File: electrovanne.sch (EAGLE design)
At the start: 11 parts, among them T1 2N2222, T2 2N2222, X1 MKDSN1,5/2-5,08

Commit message: enhanvced version
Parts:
- removed U$3: 709-SMU02N-05, mouser:709-SMU02N-05
- added C1: 0.68uF, SparkFun-Capacitors:CAP0603-CAP
- added IC1: 7805TV, linear:7805TV
- added R5: 10k, resistor:R-US_R0603
- R1: device resistor:R-EU_0207/10 -> resistor:R-US_R0603
- R2: value (none) -> 10k; device resistor:R-US_0207/10 -> resistor:R-US_R0603
- R3: value (none) -> 200; device resistor:R-US_0207/10 -> resistor:R-US_R0603
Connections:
- removed net N$7: U$4.VREF
- new net N$5: R3.2, T2.E
- net GND: now also C1.2, IC1.GND, R3.1, R5.1; no longer R2.1, T2.E, U$3.VIN-, U$3.VO-
- net N$1: now also IC1.VI, R2.2, U$4.VREF; no longer R3.2, U$3.VIN+
- net N$2: now also R5.2; no longer R2.2
- net N$8: now also R2.1; no longer R3.1
- net VCC: now also C1.1, IC1.VO; no longer U$3.VO+
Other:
- moved on the sheet: R2, R3

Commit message: 2 bugfix: (EN): dont touch to it, + the H-Bridge2 bugfix: (EN): dont touch to it, + the H-Bridge
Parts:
- removed R3: 200, resistor:R-US_R0603
- added R4: 10k, resistor:R-US_R0603
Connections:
- removed net N$5: R3.2, T2.E
- new net N$7: MS1.GPIO6, R4.2, T1.B
- net GND: now also T2.E; no longer MS1.EN, R3.1
- net N$9: now also R4.1; no longer MS1.GPIO6, T1.B
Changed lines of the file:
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@@
 <part name="GND1" library="supply1" deviceset="GND" device=""/>
 <part name="GND2" library="supply1" deviceset="GND" device=""/>
-<part name="GND3" library="supply1" deviceset="GND" device=""/>
 <part name="U$2" library="mouser" deviceset="161-0725-E" device=""/>
 <part name="GND4" library="supply1" deviceset="GND" device=""/>
@@
 <part name="R5" library="resistor" deviceset="R-US_" device="R0603" value="10k"/>
 <part name="R2" library="resistor" deviceset="R-US_" device="R0603" value="10k"/>
-<part name="R3" library="resistor" deviceset="R-US_" device="R0603" value="200"/>
 <part name="R1" library="resistor" deviceset="R-US_" device="R0603" value="10k"/>
 <part name="IC1" library="linear" deviceset="78*" device="TV" technology="05"/>
@@
 <part name="C1" library="SparkFun-Capacitors" deviceset="CAP" device="0603-CAP" value="0.68uF"/>
 <part name="GND10" library="supply1" deviceset="GND" device=""/>
+<part name="R4" library="resistor" deviceset="R-US_" device="R0603" value="10k"/>
 </parts>
 <sheets>
@@
 <instance part="GND1" gate="1" x="55.88" y="53.34"/>
 <instance part="GND2" gate="1" x="71.12" y="53.34"/>
-<instance part="GND3" gate="1" x="5.08" y="63.5" rot="R180"/>
 <instance part="U$2" gate="G$1" x="88.9" y="-15.24"/>
 <instance part="GND4" gate="1" x="2.54" y="-25.4"/>
@@
 <instance part="T1" gate="G$1" x="50.8" y="-2.54"/>
 <instance part="T2" gate="G$1" x="27.94" y="2.54"/>
-<instance part="GND5" gate="1" x="30.48" y="-22.86"/>
+<instance part="GND5" gate="1" x="30.48" y="-5.08"/>
 <instance part="R5" gate="G$1" x="53.34" y="-12.7" rot="R90"/>
 <instance part="R2" gate="G$1" x="30.48" y="12.7" rot="R90"/>
-<instance part="R3" gate="G$1" x="30.48" y="-12.7" rot="R90"/>
 <instance part="R1" gate="G$1" x="60.96" y="45.72" rot="R90"/>
 <instance part="IC1" gate="A1" x="2.54" y="-12.7" rot="MR0"/>
@@
 <instance part="C1" gate="G$1" x="-12.7" y="-17.78"/>
 <instance part="GND10" gate="1" x="-12.7" y="-25.4"/>
+<instance part="R4" gate="G$1" x="7.62" y="2.54" rot="R180"/>
 </instances>
 <busses>
@@
 </segment>
 <segment>
-<pinref part="GND3" gate="1" pin="GND"/>
-<pinref part="MS1" gate="G$1" pin="EN"/>
-<wire x1="5.08" y1="60.96" x2="10.16" y2="60.96" width="0.1524" layer="91"/>
-</segment>
-<segment>
 <pinref part="GND4" gate="1" pin="GND"/>
 <wire x1="2.54" y1="-20.32" x2="2.54" y2="-22.86" width="0.1524" layer="91"/>
@@
 </segment>
 <segment>
-<pinref part="GND5" gate="1" pin="GND"/>
-<pinref part="R3" gate="G$1" pin="1"/>
-<wire x1="30.48" y1="-20.32" x2="30.48" y2="-17.78" width="0.1524" layer="91"/>
-</segment>
-<segment>
 <pinref part="R5" gate="G$1" pin="1"/>
 <pinref part="GND6" gate="1" pin="GND"/>
@@
 <pinref part="GND10" gate="1" pin="GND"/>
 <wire x1="-12.7" y1="-22.86" x2="-12.7" y2="-20.32" width="0.1524" layer="91"/>
+</segment>
+<segment>
+<pinref part="T2" gate="G$1" pin="E"/>
+<pinref part="GND5" gate="1" pin="GND"/>
 </segment>
 </net>
@@
 </segment>
 </net>
-<net name="N$9" class="0">
-<segment>
-<pinref part="T2" gate="G$1" pin="B"/>
-<wire x1="25.4" y1="-5.08" x2="25.4" y2="2.54" width="0.1524" layer="91"/>
-<wire x1="25.4" y1="2.54" x2="-15.24" y2="2.54" width="0.1524" layer="91"/>
+<net name="N$7" class="0">
+<segment>
+<pinref part="T1" gate="G$1" pin="B"/>
+<wire x1="45.72" y1="-2.54" x2="48.26" y2="-2.54" width="0.1524" layer="91"/>
+<wire x1="45.72" y1="-7.62" x2="45.72" y2="-2.54" width="0.1524" layer="91"/>
 <pinref part="MS1" gate="G$1" pin="GPIO6"/>
 <wire x1="10.16" y1="78.74" x2="-15.24" y2="78.74" width="0.1524" layer="91"/>
 <wire x1="-15.24" y1="78.74" x2="-15.24" y2="2.54" width="0.1524" layer="91"/>
-<wire x1="25.4" y1="-5.08" x2="45.72" y2="-5.08" width="0.1524" layer="91"/>
-<pinref part="T1" gate="G$1" pin="B"/>
-<wire x1="45.72" y1="-5.08" x2="45.72" y2="-2.54" width="0.1524" layer="91"/>
-<wire x1="45.72" y1="-2.54" x2="48.26" y2="-2.54" width="0.1524" layer="91"/>
-</segment>
-</net>
-<net name="N$5" class="0">
-<segment>
-<pinref part="T2" gate="G$1" pin="E"/>
-<wire x1="30.48" y1="-2.54" x2="30.48" y2="-7.62" width="0.1524" layer="91"/>
-<pinref part="R3" gate="G$1" pin="2"/>
-</segment>
-</net>
+<wire x1="-15.24" y1="2.54" x2="-15.24" y2="-7.62" width="0.1524" layer="91"/>
+<wire x1="45.72" y1="-7.62" x2="-15.24" y2="-7.62" width="0.1524" layer="91"/>
+<wire x1="-15.24" y1="2.54" x2="2.54" y2="2.54" width="0.1524" layer="91"/>
+<pinref part="R4" gate="G$1" pin="2"/>
+</segment>
+</net>
+<net name="N$9" class="0">
+<segment>
+<pinref part="R4" gate="G$1" pin="1"/>
+<pinref part="T2" gate="G$1" pin="B"/>
+<wire x1="12.7" y1="2.54" x2="25.4" y2="2.54" width="0.1524" layer="91"/>
+</segment>
+</net>

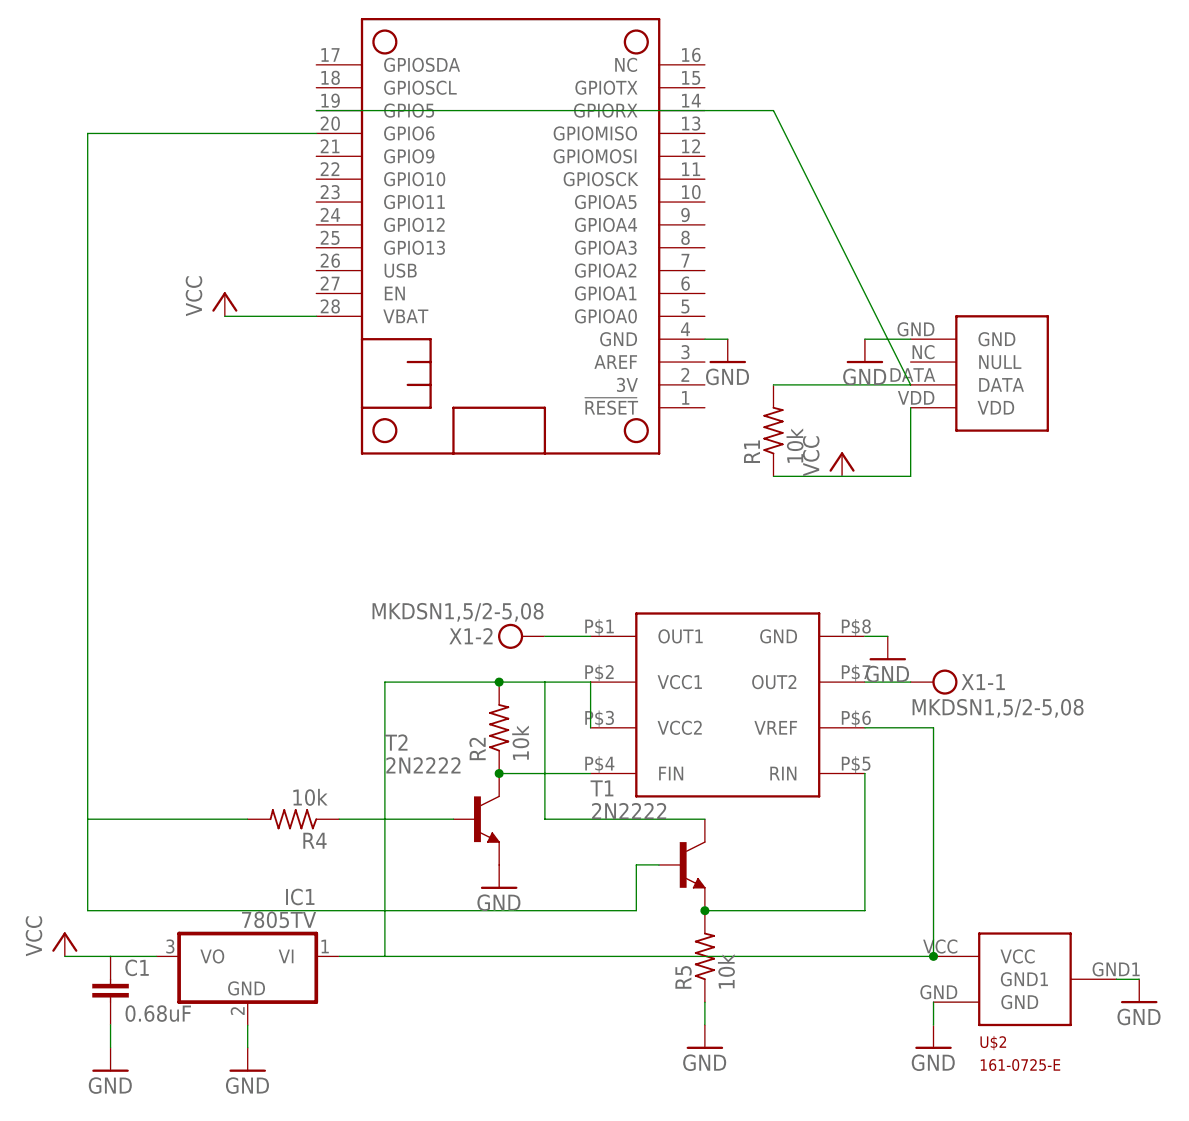
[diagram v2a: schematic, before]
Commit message: add small resistor (recommended by datasheet)
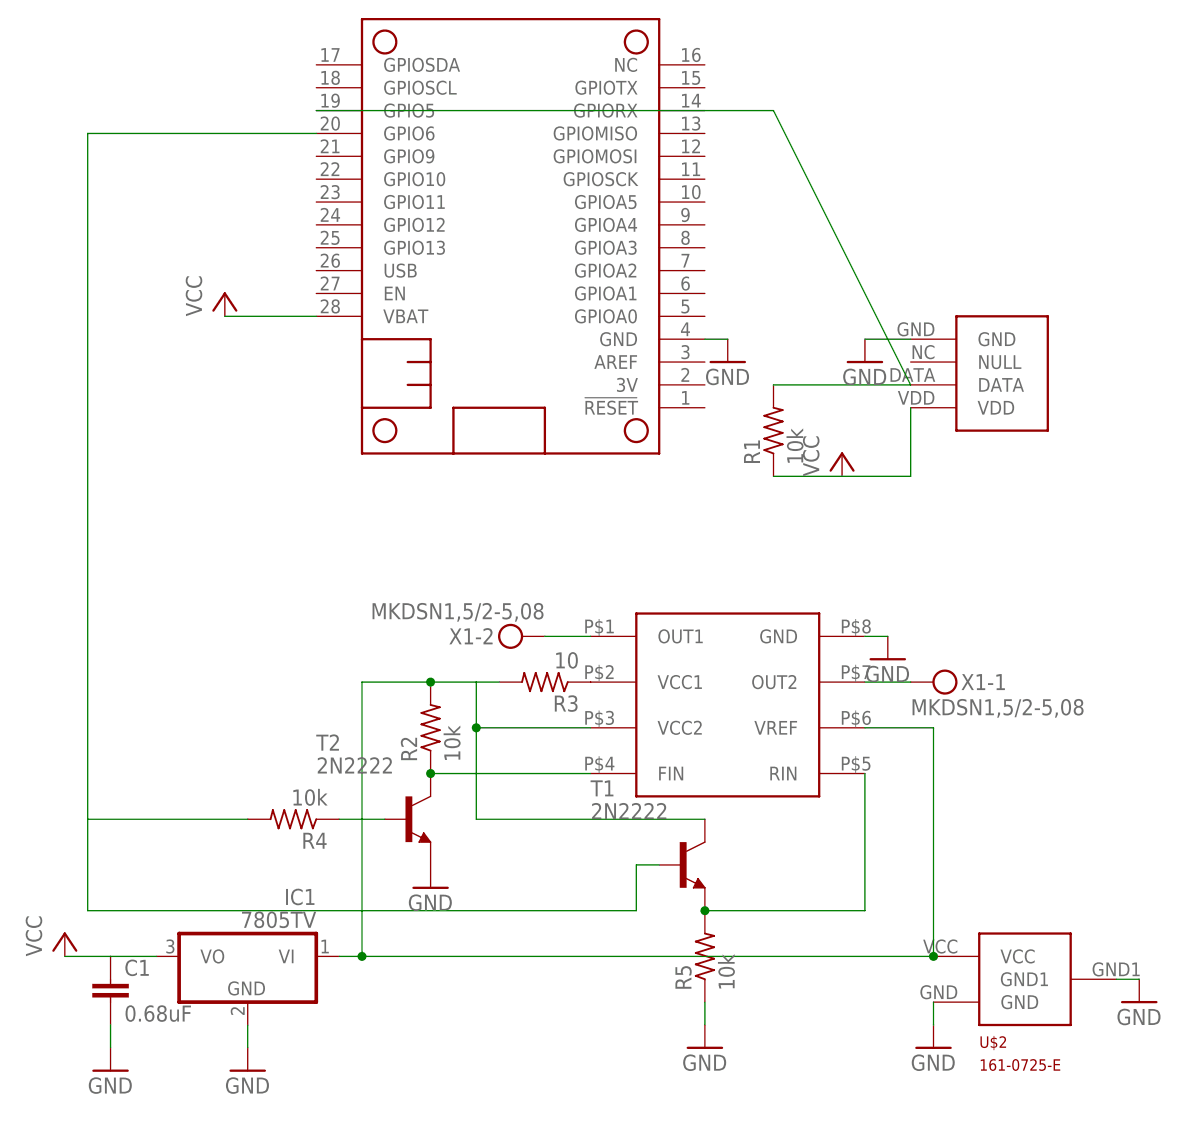
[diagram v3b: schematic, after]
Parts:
- added R3: 10, resistor:R-US_R0603
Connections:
- new net N$5: R3.1, U$4.VCC1
- net N$1: now also R3.2; no longer U$4.VCC1
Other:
- moved on the sheet: R2, T2
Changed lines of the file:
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@@
 <part name="GND10" library="supply1" deviceset="GND" device=""/>
 <part name="R4" library="resistor" deviceset="R-US_" device="R0603" value="10k"/>
+<part name="R3" library="resistor" deviceset="R-US_" device="R0603" value="10"/>
 </parts>
 <sheets>
@@
 <instance part="X1" gate="-2" x="33.02" y="22.86" rot="R180"/>
 <instance part="T1" gate="G$1" x="50.8" y="-2.54"/>
-<instance part="T2" gate="G$1" x="27.94" y="2.54"/>
-<instance part="GND5" gate="1" x="30.48" y="-5.08"/>
+<instance part="T2" gate="G$1" x="20.32" y="2.54"/>
+<instance part="GND5" gate="1" x="22.86" y="-5.08"/>
 <instance part="R5" gate="G$1" x="53.34" y="-12.7" rot="R90"/>
-<instance part="R2" gate="G$1" x="30.48" y="12.7" rot="R90"/>
+<instance part="R2" gate="G$1" x="22.86" y="12.7" rot="R90"/>
 <instance part="R1" gate="G$1" x="60.96" y="45.72" rot="R90"/>
 <instance part="IC1" gate="A1" x="2.54" y="-12.7" rot="MR0"/>
@@
 <instance part="GND10" gate="1" x="-12.7" y="-25.4"/>
 <instance part="R4" gate="G$1" x="7.62" y="2.54" rot="R180"/>
+<instance part="R3" gate="G$1" x="35.56" y="17.78" rot="R180"/>
 </instances>
 <busses>
@@
 <segment>
 <pinref part="U$2" gate="G$1" pin="VCC"/>
-<wire x1="78.74" y1="-12.7" x2="17.78" y2="-12.7" width="0.1524" layer="91"/>
-<pinref part="U$4" gate="G$1" pin="VCC1"/>
-<wire x1="17.78" y1="-12.7" x2="17.78" y2="17.78" width="0.1524" layer="91"/>
-<wire x1="17.78" y1="17.78" x2="30.48" y2="17.78" width="0.1524" layer="91"/>
-<pinref part="U$4" gate="G$1" pin="VCC2"/>
-<wire x1="30.48" y1="17.78" x2="35.56" y2="17.78" width="0.1524" layer="91"/>
-<wire x1="35.56" y1="17.78" x2="40.64" y2="17.78" width="0.1524" layer="91"/>
-<wire x1="40.64" y1="17.78" x2="40.64" y2="12.7" width="0.1524" layer="91"/>
+<wire x1="78.74" y1="-12.7" x2="15.24" y2="-12.7" width="0.1524" layer="91"/>
+<wire x1="15.24" y1="-12.7" x2="15.24" y2="17.78" width="0.1524" layer="91"/>
+<wire x1="15.24" y1="17.78" x2="22.86" y2="17.78" width="0.1524" layer="91"/>
+<wire x1="22.86" y1="17.78" x2="27.94" y2="17.78" width="0.1524" layer="91"/>
 <pinref part="T1" gate="G$1" pin="C"/>
-<wire x1="35.56" y1="17.78" x2="35.56" y2="2.54" width="0.1524" layer="91"/>
-<wire x1="35.56" y1="2.54" x2="53.34" y2="2.54" width="0.1524" layer="91"/>
+<wire x1="27.94" y1="17.78" x2="27.94" y2="12.7" width="0.1524" layer="91"/>
+<wire x1="27.94" y1="12.7" x2="27.94" y2="2.54" width="0.1524" layer="91"/>
+<wire x1="27.94" y1="2.54" x2="53.34" y2="2.54" width="0.1524" layer="91"/>
 <pinref part="R2" gate="G$1" pin="2"/>
-<junction x="30.48" y="17.78"/>
+<junction x="22.86" y="17.78"/>
 <pinref part="IC1" gate="A1" pin="VI"/>
-<wire x1="12.7" y1="-12.7" x2="17.78" y2="-12.7" width="0.1524" layer="91"/>
+<wire x1="12.7" y1="-12.7" x2="15.24" y2="-12.7" width="0.1524" layer="91"/>
 <pinref part="U$4" gate="G$1" pin="VREF"/>
 <wire x1="78.74" y1="12.7" x2="71.12" y2="12.7" width="0.1524" layer="91"/>
 <wire x1="78.74" y1="-12.7" x2="78.74" y2="12.7" width="0.1524" layer="91"/>
 <junction x="78.74" y="-12.7"/>
+<pinref part="U$4" gate="G$1" pin="VCC2"/>
+<wire x1="40.64" y1="12.7" x2="27.94" y2="12.7" width="0.1524" layer="91"/>
+<pinref part="R3" gate="G$1" pin="2"/>
+<wire x1="30.48" y1="17.78" x2="27.94" y2="17.78" width="0.1524" layer="91"/>
+<junction x="15.24" y="-12.7"/>
+<junction x="27.94" y="12.7"/>
 </segment>
 </net>
@@
 <pinref part="T2" gate="G$1" pin="C"/>
 <pinref part="U$4" gate="G$1" pin="FIN"/>
-<wire x1="30.48" y1="7.62" x2="40.64" y2="7.62" width="0.1524" layer="91"/>
+<wire x1="22.86" y1="7.62" x2="40.64" y2="7.62" width="0.1524" layer="91"/>
 <pinref part="R2" gate="G$1" pin="1"/>
-<junction x="30.48" y="7.62"/>
+<junction x="22.86" y="7.62"/>
 </segment>
 </net>
@@
 <pinref part="R4" gate="G$1" pin="1"/>
 <pinref part="T2" gate="G$1" pin="B"/>
-<wire x1="12.7" y1="2.54" x2="25.4" y2="2.54" width="0.1524" layer="91"/>
-</segment>
-</net>
+<wire x1="12.7" y1="2.54" x2="17.78" y2="2.54" width="0.1524" layer="91"/>
+</segment>
+</net>
+<net name="N$5" class="0">
+<segment>
+<pinref part="U$4" gate="G$1" pin="VCC1"/>
+<pinref part="R3" gate="G$1" pin="1"/>
+</segment>
+</net>
